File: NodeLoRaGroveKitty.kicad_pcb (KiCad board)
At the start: 2 copper layers, 45 x 50 mm, 42 parts, among them P1 PICKIT PROGRAMMER, P2 Battery, P3 A0, P4 D9, P5 USB-Serial, P6 I2C, SW1 SW_BOOT, SW2 SW_RESET, U1 AP2112, U2 MCP73831T-2ATI/OT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

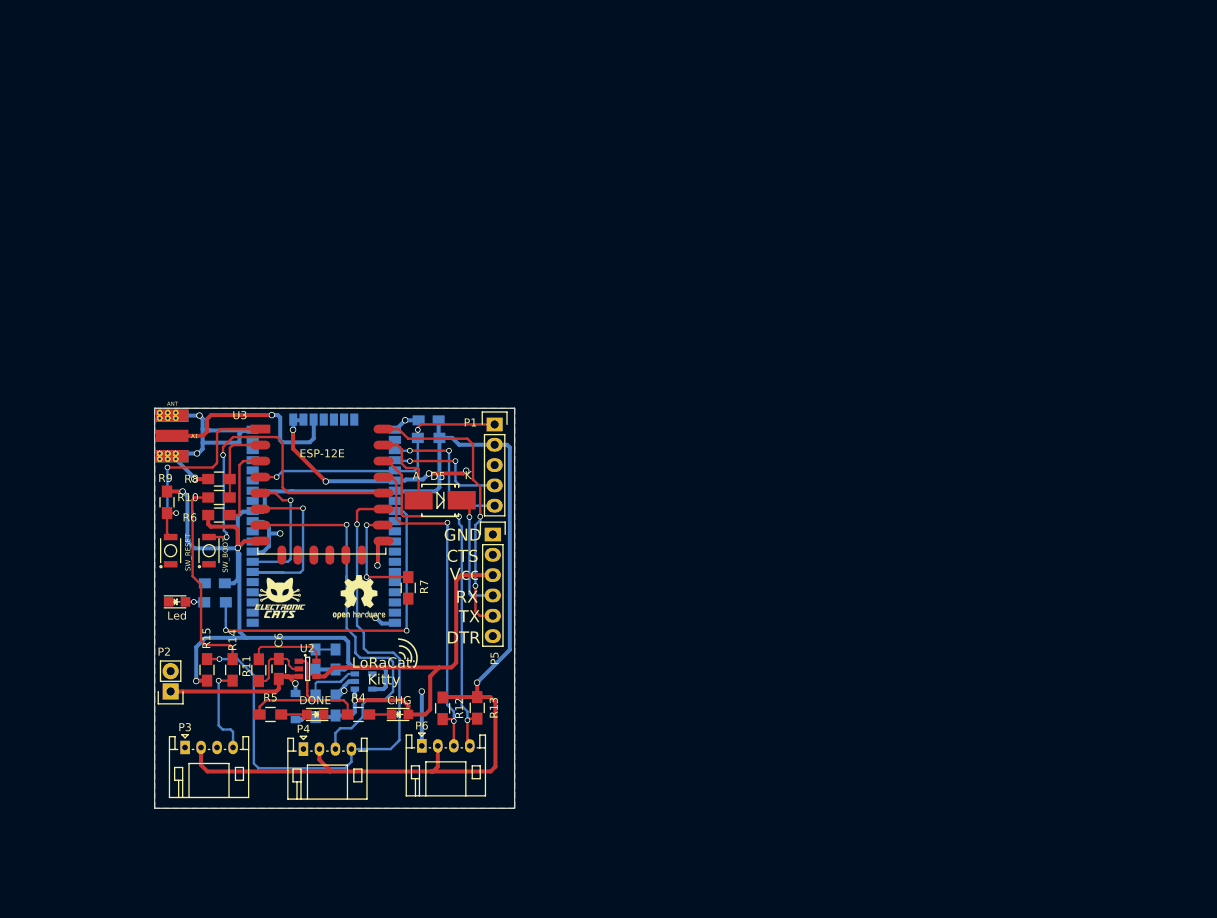
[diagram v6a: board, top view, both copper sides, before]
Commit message: Update AP2114, fix bugs JST
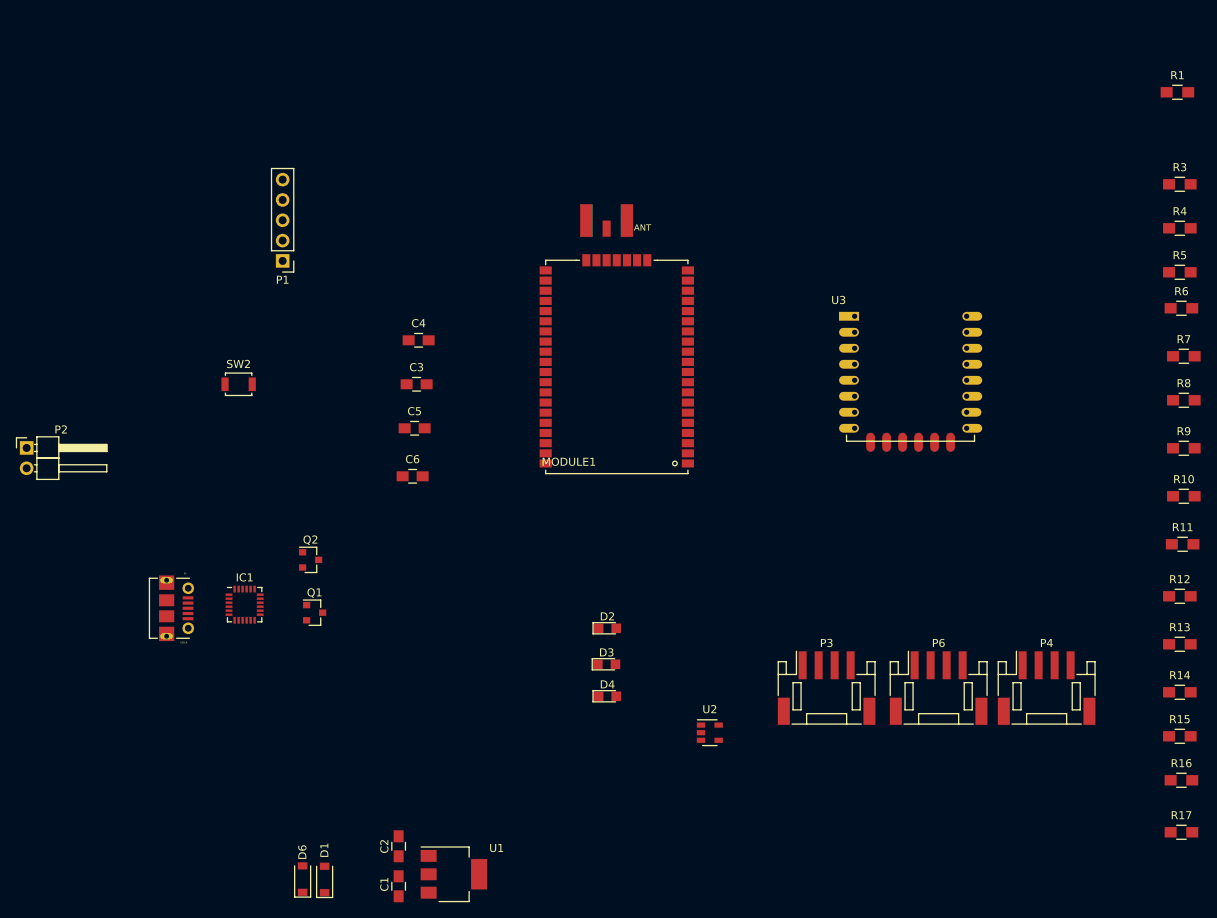
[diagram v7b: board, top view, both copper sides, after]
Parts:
- removed D5: 1N4001, Diodes_SMD:SMB_Handsoldering
- removed G***: LOGO, TIH:electronic_cats_logo_4x3
- removed R2: 100K, Resistors_SMD:R_0805_HandSoldering
- removed REF***: OSHW-Logo2_7.3x6mm_SilkScreen, Symbols:OSHW-Logo2_7.3x6mm_SilkScreen
- removed REF***: FCC-Logo_7.3x6mm_SilkScreen, Symbols:FCC-Logo_7.3x6mm_SilkScreen
- removed SW1: SW_BOOT, TIH:SW_B3U-1000P
- added D6: MBR120, Diodes_SMD:D_SOD-123, F.Cu at (120.5, 155.8)
- added IC1: CP2104, Housings_DFN_QFN:QFN-24_4x4mm_Pitch0.5mm_NoMask, F.Cu at (113.2, 121.5)
- added Q1: MMBT2222A, TO_SOT_Packages_SMD:SOT-23, F.Cu at (122.0, 122.5)
- added Q2: MMBT2222A, TO_SOT_Packages_SMD:SOT-23, F.Cu at (121.5, 116.0)
- added R16: 10K, Resistors_SMD:R_0805_HandSoldering, F.Cu at (230.3, 143.5)
- added R17: 10K, Resistors_SMD:R_0805_HandSoldering, F.Cu at (230.3, 150.0)
- A1: footprint TIH:GSG-SMA-EDGE -> Library:SMA_Conn_Ant
- C1, C2: value 10uF -> 4.7uF; moved to F.Cu
- C3: value 1uF -> 10uF; moved to F.Cu
- C4, C5, R3: moved to F.Cu
- D1: footprint Diodes_SMD:SOD-123 -> Diodes_SMD:D_SOD-123; moved to F.Cu
- MODULE1: footprint TIH:RN2483 -> Library:RN2483; moved to F.Cu
- P1: footprint Pin_Headers:Pin_Header_Straight_1x05 -> Pin_Headers:Pin_Header_Straight_1x05_Pitch2.54mm
- P2: footprint Pin_Headers:Pin_Header_Straight_1x02 -> Pin_Headers:Pin_Header_Angled_1x02_Pitch2.54mm
- P3, P4, P6: footprint Connectors_JST:JST_PH_S4B-PH-K_04x2.00mm_Angled -> Connectors_JST:JST_PH_S4B-PH-SM4-TB_04x2.00mm_Angled
- P5: value USB-Serial -> USB_B; footprint Socket_Strips:Socket_Strip_Straight_1x06 -> LoraCat:MOLEX_105017-0001
- R1: value 100R -> 330R; moved to F.Cu
- SW2: footprint TIH:SW_B3U-1000P -> Buttons_Switches_SMD:SW_SPST_B3U-1000P
- U1: value AP2112 -> AP2114; footprint TO_SOT_Packages_SMD:SOT-23-5 -> TO_SOT_Packages_SMD:SOT-223-3Lead_TabPin2; moved to F.Cu
- U3: value ESP-12E -> ESP8266-12E
- moved R1 136.1 mm to (229.8, 57.5), turned to 0 degrees
- moved R9 127.3 mm to (230.7, 102.0), turned to 0 degrees
- moved R5 126.4 mm to (230.2, 80.0)
- moved R6 123.0 mm to (230.3, 84.5)
- moved R15 121.9 mm to (230.2, 138.0), turned to 0 degrees
- moved R8 121.0 mm to (230.7, 96.0), turned to 0 degrees
- moved R10 120.6 mm to (230.7, 108.0)
- moved R4 119.3 mm to (230.2, 74.5)
- moved R14 118.4 mm to (230.2, 132.5), turned to 0 degrees
- moved R11 116.5 mm to (230.5, 114.0), turned to 0 degrees
- moved R7 101.2 mm to (230.7, 90.5), turned to 0 degrees
- moved R3 99.1 mm to (230.2, 69.0), turned to 0 degrees
- moved P4 93.2 mm to (213.5, 132.0)
- moved R12 93.2 mm to (230.2, 120.5), turned to 0 degrees
- moved R13 88.2 mm to (230.2, 126.5), turned to 0 degrees
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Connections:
- C1 pad 1: VCC -> Net-(C1-Pad1)
- D1 pad 1: VCC -> Net-(C1-Pad1)
- D2 pad 1: GND -> Net-(D2-Pad1)
- D2 pad 2: Net-(D2-Pad2) -> +3V3
- P4 pad 3: /GPIO13 -> /GPIO2
- P4 pad 4: /GPIO2 -> /GPIO13
- P5 pad 1: GND -> VCC
- P5 pad 3: VCC -> Net-(IC1-Pad3)
- P5 pad 4: /RX_5V -> GND
- P5 pad 5: /TX -> Net-(P5-Pad5)
- R1 pad 1: Net-(MODULE1-Pad36) -> /GPIO0
- R1 pad 2: Net-(D2-Pad2) -> Net-(D2-Pad1)
- U1 pad 1: VCC -> GND
- U1 pad 2: GND -> +3V3
- U1 pad 3: Net-(R2-Pad1) -> Net-(C1-Pad1)
- U3 pad 1: /RST -> /RESET
- U3 pad 10: Net-(U3-Pad10) -> /GPIO15
- U3 pad 11: Net-(U3-Pad11) -> /GPIO2
- U3 pad 12: Net-(U3-Pad12) -> /GPIO0
- U3 pad 13: Net-(U3-Pad13) -> /SDA
- U3 pad 14: Net-(U3-Pad14) -> /SCL
- U3 pad 15: GND -> /RXD
- U3 pad 16: /GPIO15 -> /TXD
- U3 pad 17: /GPIO2 -> Net-(U3-Pad17)
- U3 pad 18: /GPIO0 -> Net-(U3-Pad18)
- U3 pad 19: /SDA -> Net-(U3-Pad19)
- U3 pad 20: /SCL -> Net-(U3-Pad20)
- U3 pad 21: /RX -> Net-(U3-Pad21)
- U3 pad 22: /TX -> Net-(U3-Pad22)
- U3 pad 9: Net-(U3-Pad9) -> GND
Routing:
- net +3V3: track 230.8 -> 0.00 mm, vias 4 -> 0
- net GND: track 100.3 -> 0.00 mm, vias 13 -> 0
- net /GPIO2: track 74.0 -> 0.00 mm, vias 2 -> 0
- net VCC: track 61.4 -> 0.00 mm, vias 1 -> 0
- net /GPIO13: track 48.5 -> 0.00 mm, vias 1 -> 0
- net /SCL: track 47.0 -> 0.00 mm, vias 2 -> 0
- net /SDA: track 43.7 -> 0.00 mm, vias 2 -> 0
- net Net-(MODULE1-Pad36): track 42.2 -> 0.00 mm, vias 2 -> 0
- net /GPIO0: track 39.7 -> 0.00 mm, vias 2 -> 0
- net /TX: track 36.6 -> 0.00 mm, vias 2 -> 0
- net /RST_RN: track 34.2 -> 0.00 mm, vias 2 -> 0
- net /RST: track 32.2 -> 0.00 mm, vias 2 -> 0
- net Net-(R10-Pad1): track 26.1 -> 0.00 mm
- net Net-(A1-Pad1): track 25.2 -> 0.00 mm, vias 1 -> 0
- net /SRX: track 22.8 -> 0.00 mm, vias 1 -> 0
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- removed copper zone on B.Cu, net GND
- removed copper zone on F.Cu, net GND
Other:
- board outline removed
- board text removed: "+Batt"
- board text removed: "CTS"
- board text removed: "DTR"
- board text removed: "GND"
- board text removed: "GND VCC D13 D2"
- board text removed: "GND VCC NC A0"
- board text removed: "GND VCC SDA SCL"
- board text removed: "LoRaCat: Kitty"
- board text removed: "RX"
- board text removed: "TX"
- board text removed: "Vcc"

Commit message: New design PCB
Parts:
- removed D6: MBR120, Diodes_SMD:D_SOD-123
- removed R17: 10K, Resistors_SMD:R_0805_HandSoldering
- removed SW2: SW_RESET, Buttons_Switches_SMD:SW_SPST_B3U-1000P
- added D5: Led, LEDs:LED_0805, F.Cu at (130.0, 83.6)
- added R2: 330R, Resistors_SMD:R_0805_HandSoldering, B.Cu at (143.0, 89.8)
- added SW1: SW_RESET, Buttons_Switches_SMD:SW_SPST_B3U-1000P, F.Cu at (147.0, 68.4)
- A1, C1, C2, C5, D1, MODULE1, P1, P2, R1, R3, U1, U2: moved to B.Cu
- C3: value 10uF -> 0.1uF; moved to B.Cu
- C4: value 0.1uF -> 10uF; moved to B.Cu
- D2: value Led -> MBR120; footprint LEDs:LED_0805 -> Diodes_SMD:D_SOD-123; moved to B.Cu
- P3: value A0 -> USB_B; footprint Connectors_JST:JST_PH_S4B-PH-SM4-TB_04x2.00mm_Angled -> LoraCat:MOLEX_105017-0001
- P4: value D9 -> A0; footprint Connectors_JST:JST_PH_S4B-PH-SM4-TB_04x2.00mm_Angled -> Library:JST_PH_S4B-PH-SM4-TB_04x2.00mm_Angled
- P5: value USB_B -> D9; footprint LoraCat:MOLEX_105017-0001 -> Library:JST_PH_S4B-PH-SM4-TB_04x2.00mm_Angled
- P6: footprint Connectors_JST:JST_PH_S4B-PH-SM4-TB_04x2.00mm_Angled -> Library:JST_PH_S4B-PH-SM4-TB_04x2.00mm_Angled
- R10: value 100K -> 330R
- R11: value 10K -> 4.7K
- R13: value 4.7K -> 10K
- R14: value 100K -> 10K
- R4: value 330R -> 10K; moved to B.Cu
- R5: value 330R -> 100K
- R9: value 10K -> 100K
- moved R16 141.2 mm to (111.0, 68.1)
- moved R15 139.3 mm to (111.0, 65.8), turned to 180 degrees
- moved R14 137.7 mm to (111.0, 63.4)
- moved R9 126.5 mm to (111.0, 61.1)
- moved R8 125.3 mm to (111.0, 58.8), turned to 180 degrees
- moved R11 123.0 mm to (111.3, 83.3), turned to 270 degrees
- moved R12 122.4 mm to (113.5, 83.4), turned to 270 degrees
- moved R5 121.5 mm to (111.0, 56.5)
- moved R13 104.7 mm to (147.0, 62.8), turned to 270 degrees
- moved R10 102.9 mm to (139.1, 61.1)
- moved P6 98.5 mm to (108.8, 94.7)
- moved P4 96.0 mm to (125.0, 94.7)
- moved R4 94.2 mm to (136.7, 62.8), turned to 90 degrees
- moved R1 93.5 mm to (143.0, 92.1)
- moved R7 90.2 mm to (142.8, 69.8), turned to 270 degrees
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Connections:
- C4 pad 1: +3V3 -> +BATT
- C6 pad 1: +BATT -> +3V3
- D1 pad 2: +BATT -> VCC
- D2 pad 1: Net-(D2-Pad1) -> Net-(C1-Pad1)
- D2 pad 2: +3V3 -> +BATT
- P3 pad 1: GND -> VCC
- P3 pad 2: +3V3 -> Net-(IC1-Pad4)
- P3 pad 3: Net-(P3-Pad3) -> Net-(IC1-Pad3)
- P3 pad 4: /A0 -> GND
- P4 pad 3: /GPIO2 -> Net-(P4-Pad3)
- P4 pad 4: /GPIO13 -> /A0
- P5 pad 1: VCC -> GND
- P5 pad 2: Net-(IC1-Pad4) -> +3V3
- P5 pad 3: Net-(IC1-Pad3) -> /GPIO2
- P5 pad 4: GND -> /GPIO13
- R1 pad 1: /GPIO0 -> Net-(R1-Pad1)
- R1 pad 2: Net-(D2-Pad1) -> Net-(D3-Pad1)
- R10 pad 1: Net-(R10-Pad1) -> /GPIO0
- R10 pad 2: /ADC -> Net-(D5-Pad1)
- R11 pad 1: Net-(R11-Pad1) -> +3V3
- R11 pad 2: GND -> /SDA
- R12 pad 2: /SDA -> /SCL
- R13 pad 2: /SCL -> /RST
- R14 pad 1: /A0 -> +3V3
- R14 pad 2: Net-(R10-Pad1) -> /CH_PD
- R15 pad 1: +3V3 -> /GPIO15
- R15 pad 2: /GPIO2 -> GND
- R16 pad 1: Net-(Q1-Pad2) -> +3V3
- R16 pad 2: /RTS -> /GPIO2
- R3 pad 1: +3V3 -> Net-(R3-Pad1)
- R3 pad 2: /RST_RN -> GND
- R4 pad 1: Net-(R4-Pad1) -> +3V3
- R4 pad 2: Net-(D3-Pad1) -> /RST_RN
- R5 pad 1: Net-(R4-Pad1) -> /ADC
- R5 pad 2: Net-(D4-Pad2) -> GND
- R6 pad 1: +3V3 -> Net-(Q1-Pad2)
- R6 pad 2: /CH_PD -> /RTS
- R7 pad 1: /GPIO15 -> Net-(Q2-Pad2)
- R7 pad 2: GND -> /DTR
- R8 pad 1: /ADC -> Net-(R8-Pad1)
- R8 pad 2: GND -> /ADC
- R9 pad 1: +3V3 -> /A0
- R9 pad 2: /RST -> Net-(R8-Pad1)
- U2 pad 1: Net-(R4-Pad1) -> Net-(R1-Pad1)
- U2 pad 5: Net-(R11-Pad1) -> Net-(R3-Pad1)
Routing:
- net +BATT: track 0.00 -> 44.9 mm
- net /GPIO2: track 0.00 -> 35.9 mm
- net /GPIO15: track 0.00 -> 32.6 mm
- net GND: track 0.00 -> 27.8 mm
- net +3V3: track 0.00 -> 24.2 mm
- net Net-(A1-Pad1): track 0.00 -> 23.4 mm
- net Net-(Q1-Pad2): track 0.00 -> 15.0 mm
- net /TXD: track 0.00 -> 15.0 mm, vias 0 -> 1
- net /ADC: track 0.00 -> 13.7 mm
- net /RXD: track 0.00 -> 13.4 mm, vias 0 -> 1
- net /CH_PD: track 0.00 -> 13.4 mm
- net Net-(IC1-Pad4): track 0.00 -> 10.9 mm, vias 0 -> 2
- net Net-(C1-Pad1): track 0.00 -> 10.6 mm
- net Net-(IC1-Pad3): track 0.00 -> 7.84 mm
- net Net-(Q2-Pad2): track 0.00 -> 5.76 mm
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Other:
- board outline added: 50 x 50 mm
- board text added: "02"
- board text added: "13"
- board text added: "A0"
- board text added: "GND"
- board text added: "SCL"
- board text added: "SDA"
- board text added: "Vcc"
